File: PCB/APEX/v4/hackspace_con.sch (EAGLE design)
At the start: 13 parts

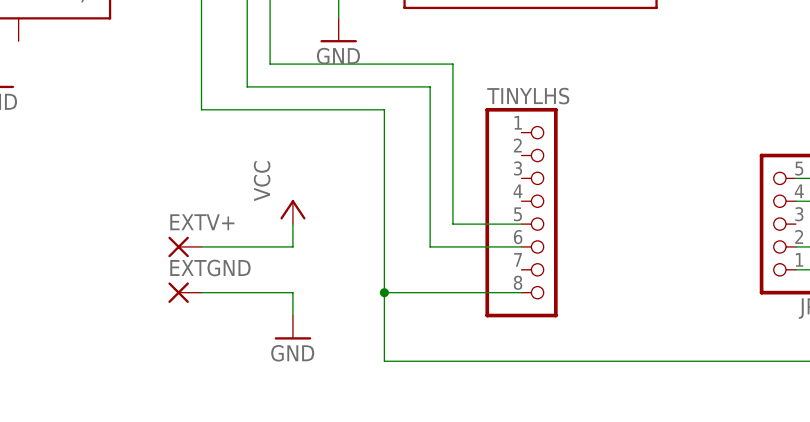
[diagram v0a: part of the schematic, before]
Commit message: ground pin 7
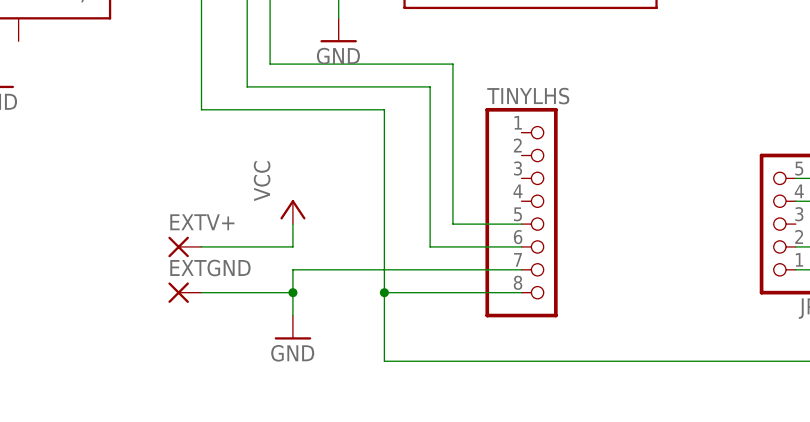
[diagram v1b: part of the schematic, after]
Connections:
- net GND: now also TINYLHS.7
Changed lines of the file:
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@@
 <pinref part="EXTGND" gate="1" pin="P"/>
 <wire x1="81.28" y1="-15.24" x2="71.12" y2="-15.24" width="0.1524" layer="91"/>
+<pinref part="TINYLHS" gate="A" pin="7"/>
+<wire x1="106.68" y1="-12.7" x2="81.28" y2="-12.7" width="0.1524" layer="91"/>
+<wire x1="81.28" y1="-12.7" x2="81.28" y2="-15.24" width="0.1524" layer="91"/>
+<junction x="81.28" y="-15.24"/>
 </segment>
 <segment>

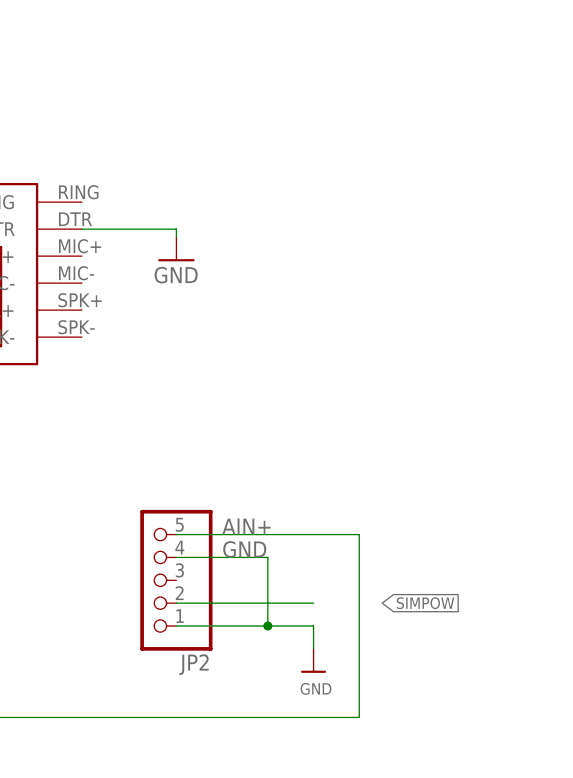
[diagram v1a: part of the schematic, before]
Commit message: embiggen pads
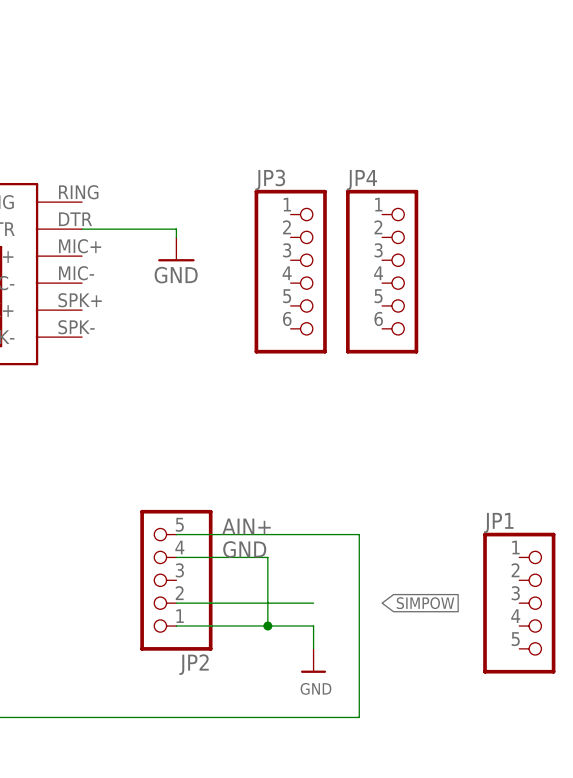
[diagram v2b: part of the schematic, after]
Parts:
- added JP1: (no value), pinhead:PINHD-1X5
- added JP3, JP4: (no value), pinhead:PINHD-1X6
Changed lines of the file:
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@@
 <part name="JP2" library="microbuilder" deviceset="HEADER-1X5" device="70MIL"/>
 <part name="U$2" library="microbuilder" deviceset="GND" device=""/>
+<part name="JP1" library="pinhead" library_urn="urn:adsk.eagle:library:325" deviceset="PINHD-1X5" device="" package3d_urn="urn:adsk.eagle:package:22469/2"/>
+<part name="JP3" library="pinhead" library_urn="urn:adsk.eagle:library:325" deviceset="PINHD-1X6" device="" package3d_urn="urn:adsk.eagle:package:22472/2"/>
+<part name="JP4" library="pinhead" library_urn="urn:adsk.eagle:library:325" deviceset="PINHD-1X6" device="" package3d_urn="urn:adsk.eagle:package:22472/2"/>
 </parts>
 <sheets>
@@
 <attribute name="VALUE" x="150.876" y="-20.32" size="1.27" layer="96"/>
 </instance>
+<instance part="JP1" gate="A" x="177.8" y="-10.16" smashed="yes">
+<attribute name="NAME" x="171.45" y="-1.905" size="1.778" layer="95"/>
+<attribute name="VALUE" x="171.45" y="-20.32" size="1.778" layer="96"/>
+</instance>
+<instance part="JP3" gate="A" x="152.4" y="25.4" smashed="yes">
+<attribute name="NAME" x="146.05" y="36.195" size="1.778" layer="95"/>
+<attribute name="VALUE" x="146.05" y="15.24" size="1.778" layer="96"/>
+</instance>
+<instance part="JP4" gate="A" x="162.56" y="25.4" smashed="yes">
+<attribute name="NAME" x="156.21" y="36.195" size="1.778" layer="95"/>
+<attribute name="VALUE" x="156.21" y="15.24" size="1.778" layer="96"/>
+</instance>
 </instances>
